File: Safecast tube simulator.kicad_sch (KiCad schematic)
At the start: 9 parts, among them Q1 IXTH10P60, SW1 SW_Push, U1 EL817, U2 EA_T123X-I2C, U3 ESP32-WROOM-32U

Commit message: Updated schematic
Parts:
- U2: value EA_T123X-I2C -> SSD1306; footprint Display:EA_T123X-I2C -> Display:SSD1306
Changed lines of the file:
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@@
       (effects (font (size 1.27 1.27)) (justify left))
     )
-    (property "Value" "EA_T123X-I2C" (at 81.28 82.0419 0)
+    (property "Value" "SSD1306" (at 81.28 82.0419 0)
       (effects (font (size 1.27 1.27)) (justify left))
     )
-    (property "Footprint" "Display:EA_T123X-I2C" (at 69.596 96.012 0)
+    (property "Footprint" "Display:SSD1306" (at 69.596 96.012 0)
       (effects (font (size 1.27 1.27)) hide)
     )
-    (property "Datasheet" "http://www.lcd-module.de/pdf/doma/t123-i2c.pdf" (at 69.596 93.472 0)
+    (property "Datasheet" "" (at 69.596 93.472 0)
       (effects (font (size 1.27 1.27)) hide)
     )
-    (property "Description" "3 Lines, 12 character alpha numeric LCD, transreflective STN and FSTN Gray, I2C, single or dual power" (at 69.596 80.772 0)
+    (property "Description" "SSD1306" (at 70.866 76.962 0)
       (effects (font (size 1.27 1.27)) hide)
     )
     (pin "1")
+    (pin "3")
     (pin "2")
-    (pin "3")
-    (pin "4")
-    (pin "5")
-    (pin "6")
+    (pin "1")
     (instances
       (project "Safecast tube simulator"

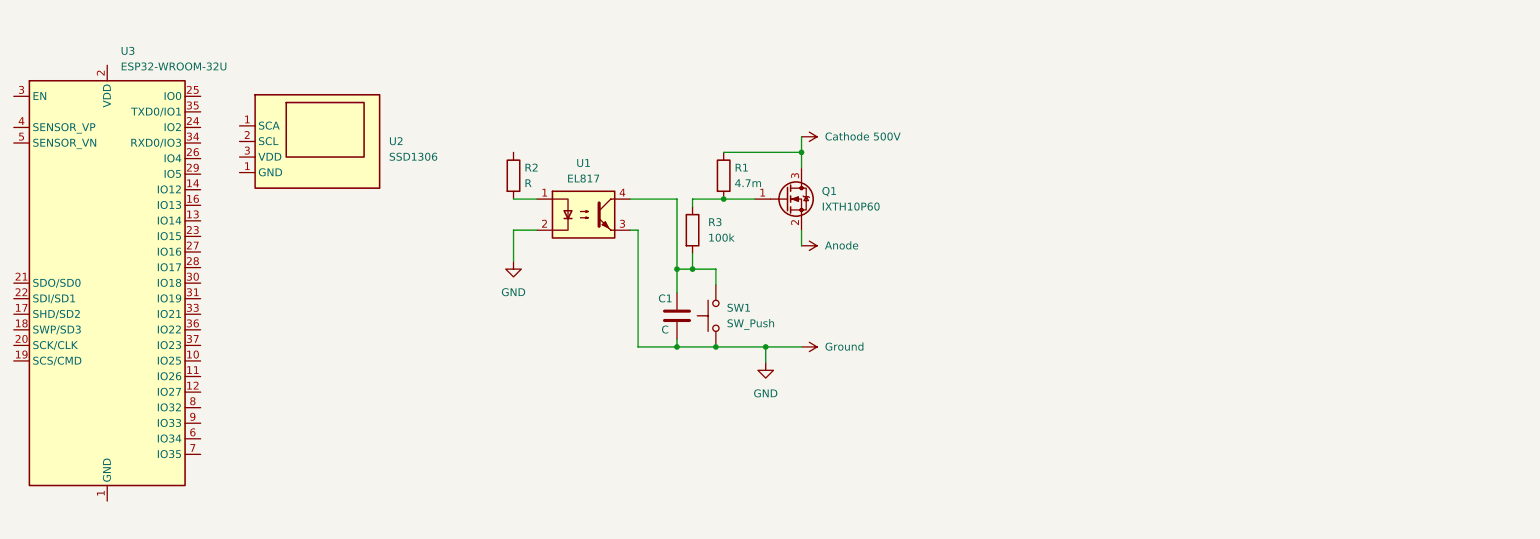
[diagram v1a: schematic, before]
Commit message: Updated OLED and rotary display
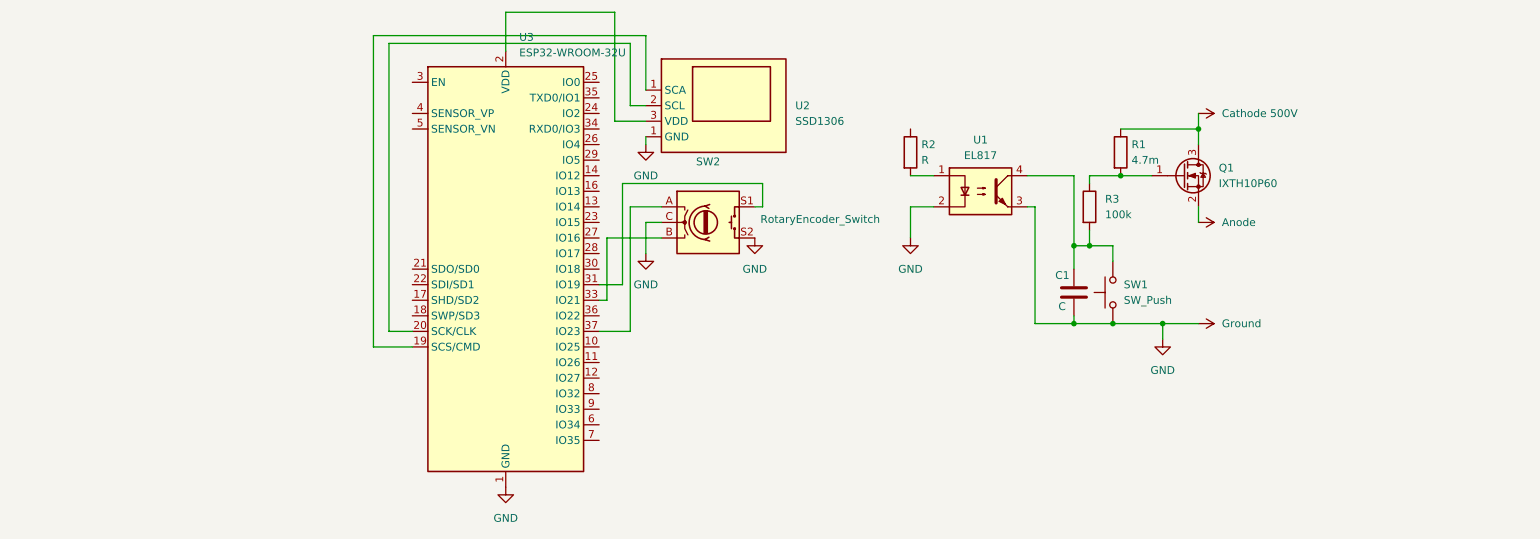
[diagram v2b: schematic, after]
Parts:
- added SW2: RotaryEncoder_Switch, symbol Device:RotaryEncoder_Switch
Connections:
- net GND: now also U2.1 (SCA), U3.1 (GND), U3.15 (GND), U3.38 (GND), U3.39 (GND), SW2.C, SW2.S2
- net at U2.2 (SCL): now also U3.20 (SCK/CLK)
- net at U2.3 (VDD): now also U3.2 (VDD)
- net at U3.19 (SCS/CMD): now also U2.1 (SCA)
- net at U3.31 (IO19): now also SW2.S1
- net at U3.33 (IO21): now also SW2.B
- net at U3.37 (IO23): now also SW2.A
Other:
- moved on the sheet: C1, Q1, R1, R2, R3, SW1, U1, U2, U3

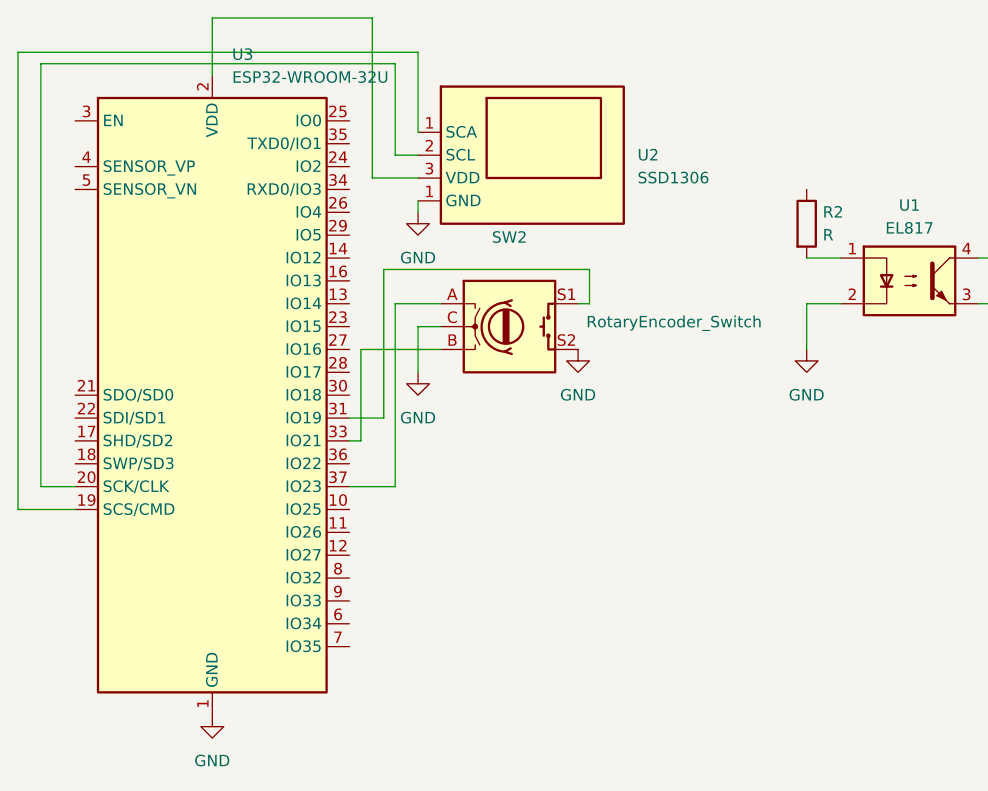
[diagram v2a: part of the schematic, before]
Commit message: updated display and interaction.
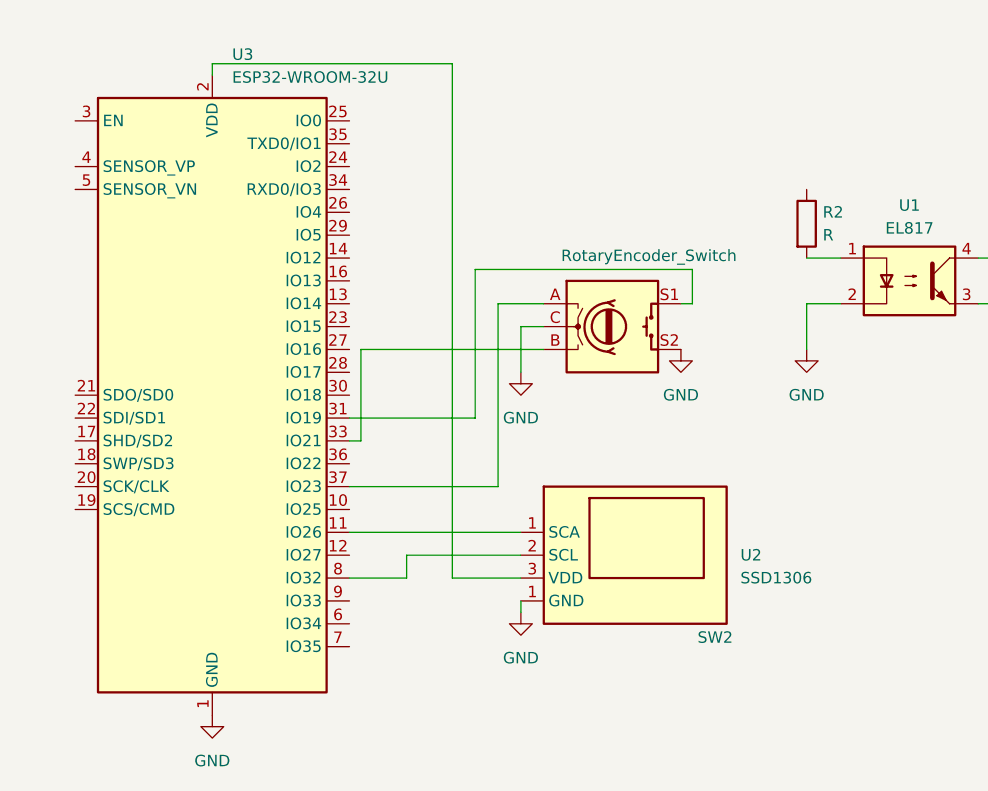
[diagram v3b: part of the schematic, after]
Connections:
- net at U3.19 (SCS/CMD): no longer U2.1 (SCA)
- net at U2.2 (SCL): now also U3.8 (IO32); no longer U3.20 (SCK/CLK)
- net at U3.11 (IO26): now also U2.1 (SCA)
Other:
- moved on the sheet: SW2, U2

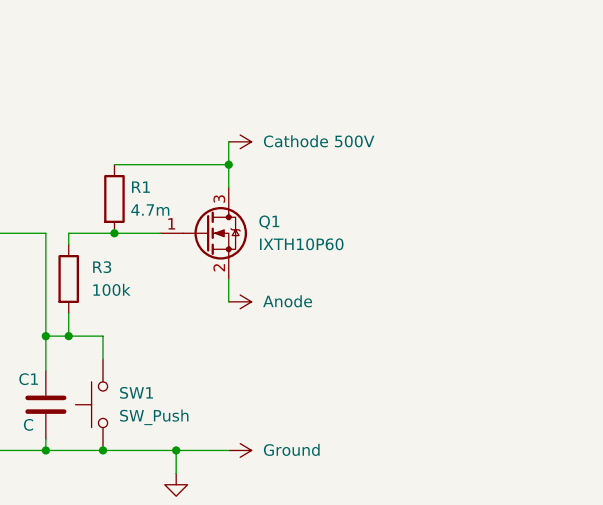
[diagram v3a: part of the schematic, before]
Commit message: Updated schematic for pull up cap.
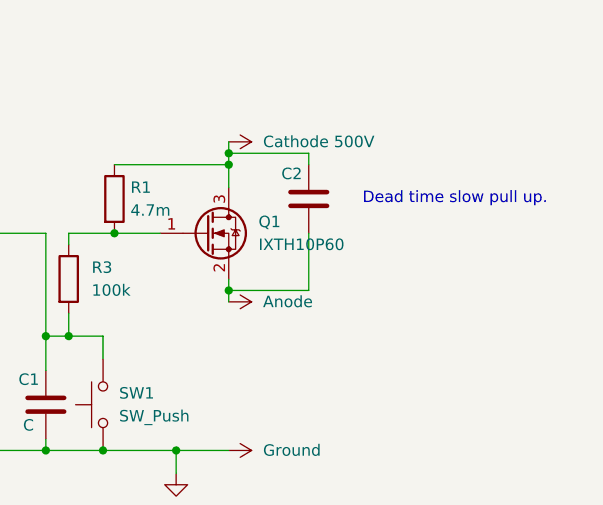
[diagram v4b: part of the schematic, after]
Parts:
- added C2: C, symbol Device:C
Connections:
- net Anode: now also C2.2
- net Cathode 500V: now also C2.1
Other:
- note added: "Dead time slow pull up."
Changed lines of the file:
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@@
 (kicad_sch (version 20230819) (generator eeschema)
   (paper "A4")
+  (junction (at 213.36 76.2) (diameter 0) (color 0 0 0 0)
+  )
   (junction (at 200.66 85.09) (diameter 0) (color 0 0 0 0)
   )
@@
   (junction (at 195.58 96.52) (diameter 0) (color 0 0 0 0)
   )
+  (junction (at 213.36 91.44) (diameter 0) (color 0 0 0 0)
+  )
   (junction (at 213.36 77.47) (diameter 0) (color 0 0 0 0)
   )
@@
     (stroke (width 0) (type default))
   )
+  (wire (pts (xy 222.25 85.09) (xy 222.25 91.44))
+    (stroke (width 0) (type default))
+  )
   (wire (pts (xy 100.33 63.5) (xy 100.33 64.77))
     (stroke (width 0) (type default))
   )
+  (wire (pts (xy 213.36 91.44) (xy 213.36 92.71))
+    (stroke (width 0) (type default))
+  )
   (wire (pts (xy 132.08 90.17) (xy 132.08 110.49))
     (stroke (width 0) (type default))
   )
+  (wire (pts (xy 222.25 91.44) (xy 213.36 91.44))
+    (stroke (width 0) (type default))
+  )
   (wire (pts (xy 207.518 109.22) (xy 213.36 109.22))
     (stroke (width 0) (type default))
@@
     (stroke (width 0) (type default))
   )
+  (wire (pts (xy 213.36 76.2) (xy 213.36 77.47))
+    (stroke (width 0) (type default))
+  )
   (wire (pts (xy 186.69 109.22) (xy 193.04 109.22))
     (stroke (width 0) (type default))
@@
     (stroke (width 0) (type default))
   )
-  (wire (pts (xy 213.36 74.93) (xy 213.36 77.47))
+  (wire (pts (xy 213.36 74.93) (xy 213.36 76.2))
     (stroke (width 0) (type default))
   )
@@
     (stroke (width 0) (type default))
   )
+  (wire (pts (xy 222.25 77.47) (xy 222.25 76.2))
+    (stroke (width 0) (type default))
+  )
   (wire (pts (xy 166.37 90.17) (xy 166.37 95.25))
     (stroke (width 0) (type default))
@@
     (stroke (width 0) (type default))
   )
+  (wire (pts (xy 222.25 76.2) (xy 213.36 76.2))
+    (stroke (width 0) (type default))
+  )
   (wire (pts (xy 213.36 77.47) (xy 213.36 80.01))
     (stroke (width 0) (type default))
@@
     (stroke (width 0) (type default))
   )
-  (wire (pts (xy 213.36 90.17) (xy 213.36 92.71))
+  (wire (pts (xy 213.36 90.17) (xy 213.36 91.44))
     (stroke (width 0) (type default))
   )
@@
   (wire (pts (xy 195.58 85.09) (xy 200.66 85.09))
     (stroke (width 0) (type default))
+  )
+  (text "Dead time slow pull up." (exclude_from_sim no)
+ (at 238.506 81.28 0)
+    (effects (font (size 1.27 1.27)))
   )
   (symbol (lib_id "Device:RotaryEncoder_Switch") (at 144.78 92.71 0) (unit 1)
@@
         )
       )
+    )
+  )
+  (symbol (lib_id "Device:C") (at 222.25 81.28 0) (unit 1)
+    (exclude_from_sim no) (in_bom yes) (on_board yes) (dnp no)
+    (property "Reference" "C2" (at 219.202 78.486 0)
+      (effects (font (size 1.27 1.27)) (justify left))
+    )
+    (property "Value" "C" (at 224.536 78.486 0)
+      (effects (font (size 1.27 1.27)) (justify left) hide)
+    )
+    (property "Footprint" "" (at 223.2152 85.09 0)
+      (effects (font (size 1.27 1.27)) hide)
+    )
+    (property "Datasheet" "~" (at 222.25 81.28 0)
+      (effects (font (size 1.27 1.27)) hide)
+    )
+    (property "Description" "Unpolarized capacitor" (at 222.25 81.28 0)
+      (effects (font (size 1.27 1.27)) hide)
+    )
+    (pin "1")
+    (pin "2")
+    (instances
+      (project "Safecast tube simulator"
+        (path "/757f8051-c0f1-48f3-a28e-7f57f8c03b8d"
+          (reference "C2") (unit 1)
+        )
+      )
